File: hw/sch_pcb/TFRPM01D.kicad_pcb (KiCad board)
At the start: 2 copper layers, 37.5 x 19 mm, 24 parts, among them J1 HEADER_1x03, J2 SM04B-GHS-TB, J3 SM04B-GHS-TB, M2 M3, U1 PCF8583, U2 SN74LVC1G14-Q1, U3 MIC5504-3.3YM5

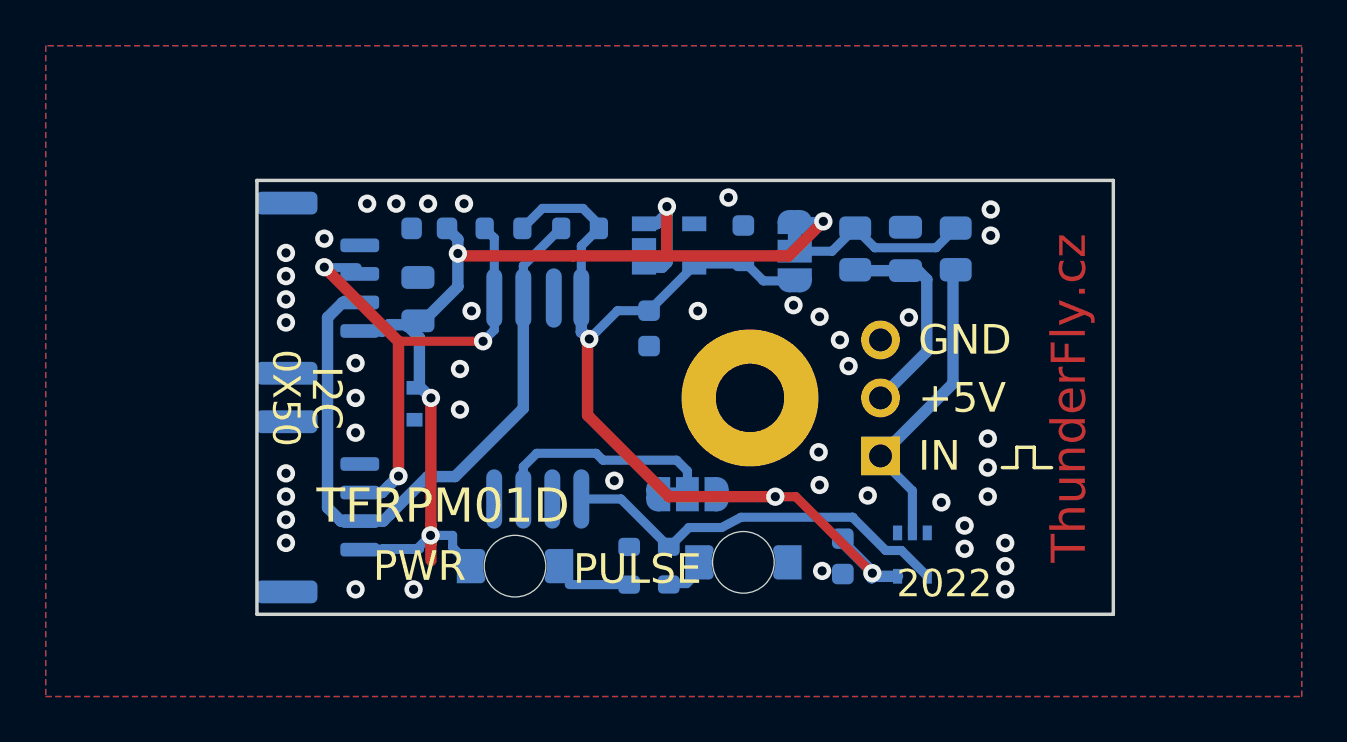
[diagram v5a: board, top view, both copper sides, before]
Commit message: Edit PCB. LED footprint. 10uF 0805 to 0603
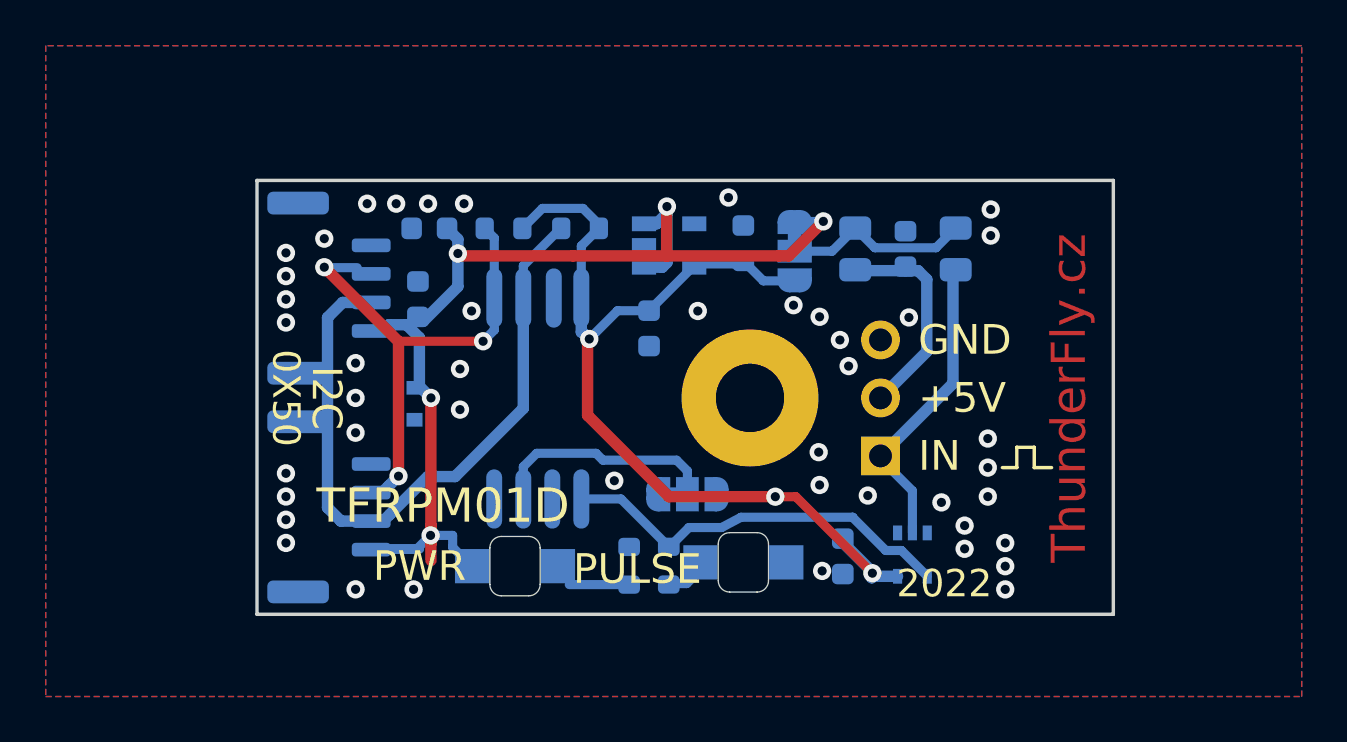
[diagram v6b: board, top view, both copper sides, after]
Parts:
- C2, C3: footprint Capacitor_SMD:C_0805_2012Metric -> Capacitor_SMD:C_0603_1608Metric
- D2, D3: footprint Mlab_D:LED_1206 -> Mlab_D:LED_1206_2
- moved J2 0.50 mm to (114.2, 127.5)
- moved J3 0.50 mm to (114.2, 137.1)

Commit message: Edit
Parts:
- moved D2 0.29 mm to (132.6, 139.5)
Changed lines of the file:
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@@
   )
   (footprint "Mlab_D:LED_1206_2" (layer "B.Cu")
-    (at 132.298 139.531096)
+    (at 132.588 139.531096)
     (descr "Diode Mini-MELF Standard")
     (tags "Diode Mini-MELF Standard")
@@
       (effects (font (size 1 1) (thickness 0.15)))
     )
-    (fp_line (start -0.6 1.3) (end 0.6 1.3) (layer "Edge.Cuts") (width 0.05))
-    (fp_line (start -1.1 -0.8) (end -1.1 0.8) (layer "Edge.Cuts") (width 0.05))
-    (fp_line (start -0.6 -1.3) (end 0.6 -1.3) (layer "Edge.Cuts") (width 0.05))
-    (fp_line (start 1.1 -0.8) (end 1.1 0.8) (layer "Edge.Cuts") (width 0.05))
-    (fp_arc (start -1.1 -0.8) (mid -0.953553 -1.153553) (end -0.6 -1.3) (layer "Edge.Cuts") (width 0.05))
-    (fp_arc (start -0.6 1.3) (mid -0.953553 1.153553) (end -1.1 0.8) (layer "Edge.Cuts") (width 0.05))
-    (fp_arc (start 1.1 0.8) (mid 0.953553 1.153553) (end 0.6 1.3) (layer "Edge.Cuts") (width 0.05))
-    (fp_arc (start 0.6 -1.3) (mid 0.953553 -1.153553) (end 1.1 -0.8) (layer "Edge.Cuts") (width 0.05))
+    (fp_line (start 1.1 -0.7) (end 1.1 0.7) (layer "Edge.Cuts") (width 0.05))
+    (fp_line (start -0.6 1.2) (end 0.6 1.2) (layer "Edge.Cuts") (width 0.05))
+    (fp_line (start -0.6 -1.2) (end 0.6 -1.2) (layer "Edge.Cuts") (width 0.05))
+    (fp_line (start -1.1 -0.7) (end -1.1 0.7) (layer "Edge.Cuts") (width 0.05))
+    (fp_arc (start -0.6 1.2) (mid -0.953553 1.053553) (end -1.1 0.7) (layer "Edge.Cuts") (width 0.05))
+    (fp_arc (start 1.1 0.7) (mid 0.953553 1.053553) (end 0.6 1.2) (layer "Edge.Cuts") (width 0.05))
+    (fp_arc (start 0.6 -1.2) (mid 0.953553 -1.053553) (end 1.1 -0.7) (layer "Edge.Cuts") (width 0.05))
+    (fp_arc (start -1.1 -0.7) (mid -0.953553 -1.053553) (end -0.6 -1.2) (layer "Edge.Cuts") (width 0.05))
+    (fp_line (start -2.5146 -1.4224) (end -2.5146 1.4224) (layer "B.Fab") (width 0.15))
+    (fp_line (start -2.4638 1.4224) (end 2.4892 1.4224) (layer "B.Fab") (width 0.15))
     (fp_line (start 2.4384 -1.4224) (end -2.5146 -1.4224) (layer "B.Fab") (width 0.15))
-    (fp_line (start -2.4638 1.4224) (end 2.4892 1.4224) (layer "B.Fab") (width 0.15))
     (fp_line (start 2.5146 1.4224) (end 2.5146 -1.4224) (layer "B.Fab") (width 0.15))
-    (fp_line (start -2.5146 -1.4224) (end -2.5146 1.4224) (layer "B.Fab") (width 0.15))
     (pad "1" smd rect (at 1.88 0 180) (size 1.5 1.5) (layers "B.Cu" "B.Paste" "B.Mask")
       (net 1 "GND") (pinfunction "K") (pintype "passive"))
@@
       (effects (font (size 1.524 1.524) (thickness 0.3048)) (justify mirror))
     )
+    (fp_text user "${REFERENCE}" (at 0 0 180) (layer "B.Fab")
+      (effects (font (size 1.27 1.27) (thickness 0.15)) (justify mirror))
+    )
     (fp_text user "K" (at 1.8542 -0.0508 180) (layer "B.Fab")
-      (effects (font (size 1.27 1.27) (thickness 0.15)) (justify mirror))
-    )
-    (fp_text user "${REFERENCE}" (at 0 0 180) (layer "B.Fab")
       (effects (font (size 1.27 1.27) (thickness 0.15)) (justify mirror))
     )
@@
       (effects (font (size 1 1) (thickness 0.15)))
     )
-    (fp_line (start -0.6 -1.3) (end 0.6 -1.3) (layer "Edge.Cuts") (width 0.05))
-    (fp_line (start 1.1 -0.8) (end 1.1 0.8) (layer "Edge.Cuts") (width 0.05))
-    (fp_line (start -1.1 -0.8) (end -1.1 0.8) (layer "Edge.Cuts") (width 0.05))
-    (fp_line (start -0.6 1.3) (end 0.6 1.3) (layer "Edge.Cuts") (width 0.05))
-    (fp_arc (start 1.1 0.8) (mid 0.953553 1.153553) (end 0.6 1.3) (layer "Edge.Cuts") (width 0.05))
-    (fp_arc (start -1.1 -0.8) (mid -0.953553 -1.153553) (end -0.6 -1.3) (layer "Edge.Cuts") (width 0.05))
-    (fp_arc (start 0.6 -1.3) (mid 0.953553 -1.153553) (end 1.1 -0.8) (layer "Edge.Cuts") (width 0.05))
-    (fp_arc (start -0.6 1.3) (mid -0.953553 1.153553) (end -1.1 0.8) (layer "Edge.Cuts") (width 0.05))
+    (fp_line (start -0.6 -1.2) (end 0.6 -1.2) (layer "Edge.Cuts") (width 0.05))
+    (fp_line (start -1.1 -0.7) (end -1.1 0.7) (layer "Edge.Cuts") (width 0.05))
+    (fp_line (start -0.6 1.2) (end 0.6 1.2) (layer "Edge.Cuts") (width 0.05))
+    (fp_line (start 1.1 -0.7) (end 1.1 0.7) (layer "Edge.Cuts") (width 0.05))
+    (fp_arc (start 1.1 0.7) (mid 0.953553 1.053553) (end 0.6 1.2) (layer "Edge.Cuts") (width 0.05))
+    (fp_arc (start 0.6 -1.2) (mid 0.953553 -1.053553) (end 1.1 -0.7) (layer "Edge.Cuts") (width 0.05))
+    (fp_arc (start -1.1 -0.7) (mid -0.953553 -1.053553) (end -0.6 -1.2) (layer "Edge.Cuts") (width 0.05))
+    (fp_arc (start -0.6 1.2) (mid -0.953553 1.053553) (end -1.1 0.7) (layer "Edge.Cuts") (width 0.05))
     (fp_line (start 2.4384 -1.4224) (end -2.5146 -1.4224) (layer "B.Fab") (width 0.15))
     (fp_line (start 2.5146 1.4224) (end 2.5146 -1.4224) (layer "B.Fab") (width 0.15))

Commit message: Edit
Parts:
- added FID1: Fiducial, Fiducial:Fiducial_0.5mm_Mask1.5mm, B.Cu at (146.1, 125.8)
- added FID2: Fiducial, Fiducial:Fiducial_0.5mm_Mask1.5mm, B.Cu at (146.1, 139.3)
- added FID3: Fiducial, Fiducial:Fiducial_0.5mm_Mask1.5mm, B.Cu at (118.6, 140.3)
- added G1: LOGO, MLAB_LOGA:TF, F.Cu at (122.2, 127.3)
- JP1: moved to F.Cu
- moved JP1 7.25 mm to (124.0, 132.3)
- moved C3 3.09 mm to (117.6, 131.1), turned to 180 degrees
- moved R5 0.84 mm to (126.5, 139.4)
- moved D1 0.81 mm to (117.6, 133.3), turned to 180 degrees
- moved U1 0.79 mm to (123.3, 131.6)
- moved R4 0.56 mm to (128.5, 139.4)
- moved C6 0.50 mm to (136.4, 139.7)
- moved D3 0.47 mm to (122.6, 139.3)
- moved D2 0.20 mm to (132.6, 139.3)
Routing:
- net Net-(JP1-Pad2): track 10.2 -> 4.17 mm, vias 0 -> 1
- net +3V3: track 44.0 -> 39.6 mm, vias 3 -> 2
- net +5V: track 51.6 -> 49.5 mm
- net /SDA: track 23.0 -> 23.7 mm
- net Net-(R4-Pad1): track 17.9 -> 18.5 mm
- net GND: vias 44 -> 58
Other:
- rule pad_to_mask_clearance: 0 -> 0.2
- board text added: "0X50 0X51"
- board text removed: "0X50"
